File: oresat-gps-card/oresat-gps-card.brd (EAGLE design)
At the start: 99.8 x 94.6 mm, 374 parts, among them J1 ORESAT-DEBUG-CONNECTOR-CARD, J100 DM3BT-DSF-PEJS, J102 FTSH-105-XX-X-DV-K, J4 TFM-120-01-L-D-RA, Q1 MMBT2907, Q2 PMV45EN, Q3 DMP2240UDM, Q4 PMV45EN, Q5 MOSFET-PCH-SOT23-6, Q6 MOSFET-PCH-SOT23-6, U1 RCLAMP0504FB, U10 TLVH431, U11 TCAN330, U12 MIC842LYC5, U13 MIC842LYC5, U14 MAX4211FETE, U15 TPS62112, U16 MAX7310ATE, U17 25AAXX, U18 RCLAMP0504FB, U19 BP2G+, U2 TPS2051CDBVR, U20 MAX8510EXK29+T, U22 LT1719S6, U4 SN74LVC1G07DCK, U5 SKY65723-81, U6 7Q-16.368MBG-T, U7 OSD3358-512M-BSM, U8 MAX8510EXK29+T, U9 MAX8510EXK29+T, Y1 24MHz, Y2 ABS07-32.768KHZ-T

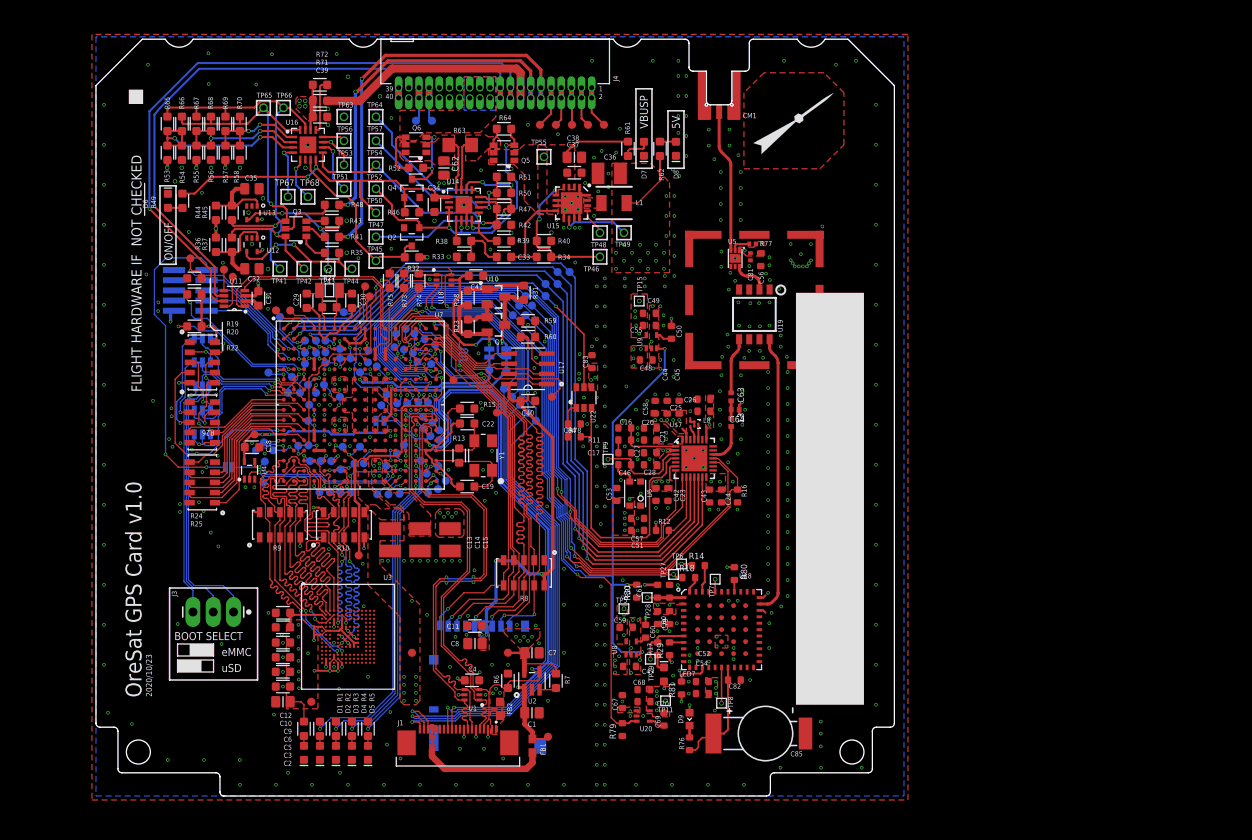
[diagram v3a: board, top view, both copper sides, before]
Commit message: Updated boot circuitry. Cleaned up names layer.
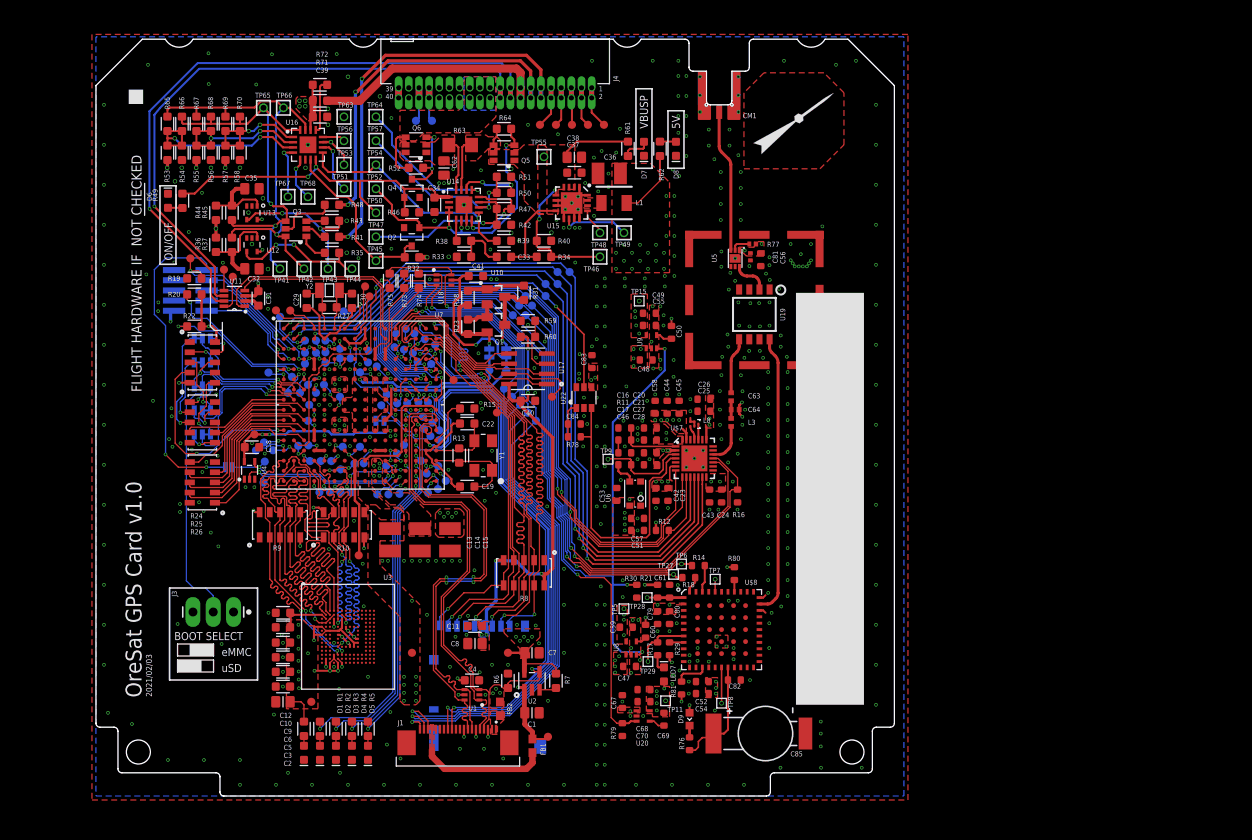
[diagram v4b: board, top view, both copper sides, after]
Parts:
- JP107: value JUMPER-SMT_3_NO_SILK -> JUMPER-SMT_3_1-NC_TRACE_SILK; device SparkFun-Jumpers:SMT-JUMPER_3_NO_SILK -> SparkFun-Jumpers:SMT-JUMPER_3_1-NC_TRACE_SILK
- L8: value SF14-1575F5UU19 -> SF14-1575F5UUA1
- moved TP29 0.42 mm to (69.0, 16.8)
- moved TP182 0.10 mm to (31.0, 60.6)
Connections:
- net 3.3V: now also J3.1
- net GND: now also J3.3
- net N$109: now also JP107.3; no longer J3.1, JP107.1
- net N$631: now also JP107.1; no longer J3.3, JP107.3
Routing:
- net N$109: track 38.5 -> 4.56 mm
- net N$631: track 30.4 -> 4.07 mm
- net MAX-CLKOUT: track 46.8 -> 46.2 mm
- net GND: vias 502 -> 508
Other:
- board text added: "2021/02/03"
- board text removed: "2020/10/23"
